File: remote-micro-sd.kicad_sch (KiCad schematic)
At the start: 0 parts

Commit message: Include adg774a component lib
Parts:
- added IC1: ADG774ABRQZ, SOP64P600X175-16N, symbol adg774a:ADG774ABRQZ
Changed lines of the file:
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@@
 	(generator_version "9.0")
 	(paper "A4")
+	(symbol
+		(lib_id "adg774a:ADG774ABRQZ")
+		(at 93.98 81.28 0)
+		(unit 1)
+		(exclude_from_sim no)
+		(in_bom yes)
+		(on_board yes)
+		(dnp no)
+		(fields_autoplaced yes)
+		(property "Reference" "IC1"
+			(at 106.68 73.66 0)
+			(effects
+				(font
+					(size 1.27 1.27)
+				)
+			)
+		)
+		(property "Value" "ADG774ABRQZ"
+			(at 106.68 76.2 0)
+			(effects
+				(font
+					(size 1.27 1.27)
+				)
+			)
+		)
+		(property "Footprint" "SOP64P600X175-16N"
+			(at 115.57 176.2 0)
+			(effects
+				(font
+					(size 1.27 1.27)
+				)
+				(justify left top)
+				(hide yes)
+			)
+		)
+		(property "Datasheet" "http://www.analog.com/media/en/technical-documentation/data-sheets/ADG774A.pdf"
+			(at 115.57 276.2 0)
+			(effects
+				(font
+					(size 1.27 1.27)
+				)
+				(justify left top)
+				(hide yes)
+			)
+		)
+		(property "Description" "ADG774ABRQZ analogue switch, QSOP16 Analog Devices ADG774ABRQZ, Analogue Switch Quad 2:1, 3.3 V, 5 V, 16-Pin QSOP"
+			(at 93.98 81.28 0)
+			(effects
+				(font
+					(size 1.27 1.27)
+				)
+				(hide yes)
+			)
+		)
+		(property "Height" "1.75"
+			(at 115.57 476.2 0)
+			(effects
+				(font
+					(size 1.27 1.27)
+				)
+				(justify left top)
+				(hide yes)
+			)
+		)
+		(property "Manufacturer_Name" "Analog Devices"
+			(at 115.57 576.2 0)
+			(effects
+				(font
+					(size 1.27 1.27)
+				)
+				(justify left top)
+				(hide yes)
+			)
+		)
+		(property "Manufacturer_Part_Number" "ADG774ABRQZ"
+			(at 115.57 676.2 0)
+			(effects
+				(font
+					(size 1.27 1.27)
+				)
+				(justify left top)
+				(hide yes)
+			)
+		)
+		(property "Mouser Part Number" "584-ADG774ABRQZ"
+			(at 115.57 776.2 0)
+			(effects
+				(font
+					(size 1.27 1.27)
+				)
+				(justify left top)
+				(hide yes)
+			)
+		)
+		(property "Mouser Price/Stock" "https://www.mouser.co.uk/ProductDetail/Analog-Devices/ADG774ABRQZ?qs=BpaRKvA4VqET7XGcXCMwIA%3D%3D"
+			(at 115.57 876.2 0)
+			(effects
+				(font
+					(size 1.27 1.27)
+				)
+				(justify left top)
+				(hide yes)
+			)
+		)
+		(property "Arrow Part Number" "ADG774ABRQZ"
+			(at 115.57 976.2 0)
+			(effects
+				(font
+					(size 1.27 1.27)
+				)
+				(justify left top)
+				(hide yes)
+			)
+		)
+		(property "Arrow Price/Stock" "https://www.arrow.com/en/products/adg774abrqz/analog-devices?region=nac"
+			(at 115.57 1076.2 0)
+			(effects
+				(font
+					(size 1.27 1.27)
+				)
+				(justify left top)
+				(hide yes)
+			)
+		)
+		(pin "16"
+		)
+		(pin "11"
+		)
+		(pin "8"
+		)
+		(pin "13"
+		)
+		(pin "10"
+		)
+		(pin "12"
+		)
+		(pin "14"
+		)
+		(pin "9"
+		)
+		(pin "15"
+		)
+		(pin "7"
+		)
+		(pin "2"
+		)
+		(pin "3"
+		)
+		(pin "4"
+		)
+		(pin "5"
+		)
+		(pin "6"
+		)
+		(pin "1"
+		)
+		(instances
+			(project ""
+				(path "/fc3ce78a-41c8-4e03-a9e4-6557f1cd3bfd"
+					(reference "IC1")
+					(unit 1)
+				)
+			)
+		)
+	)
 	(sheet_instances
 		(path "/"

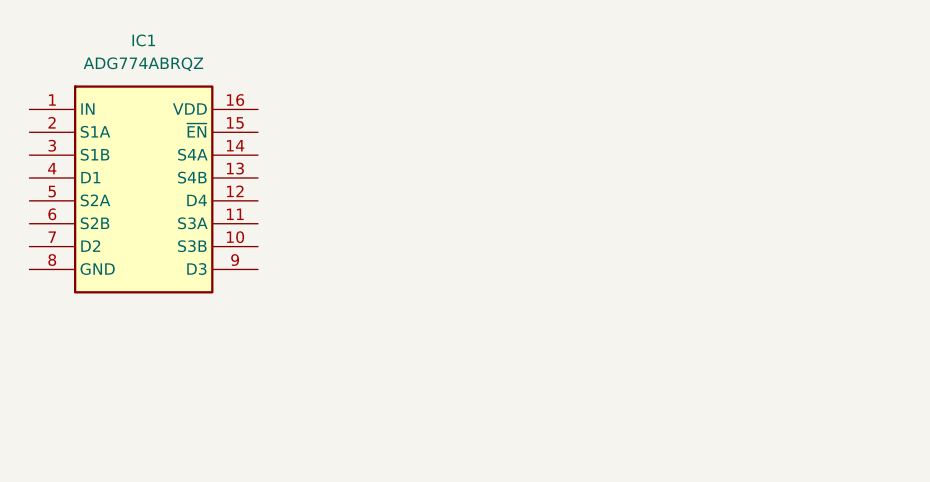
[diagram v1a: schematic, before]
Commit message: Integrate adg774a and supermini to the project
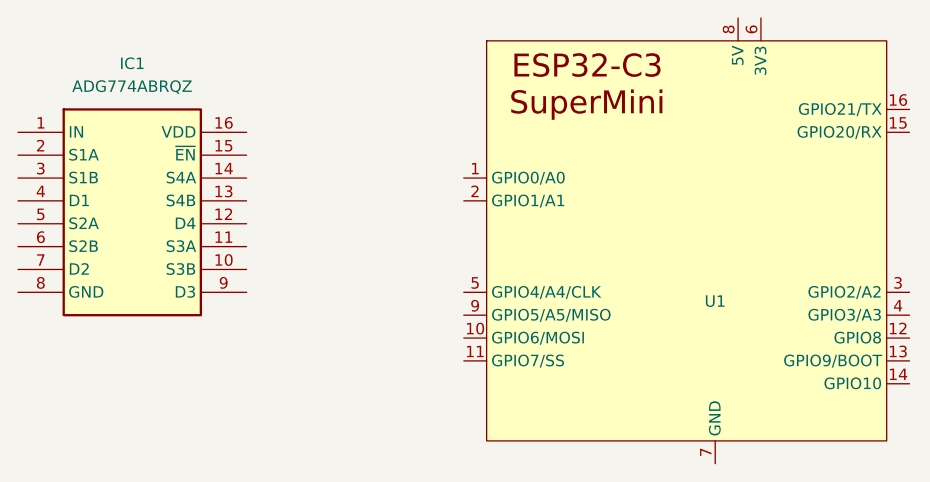
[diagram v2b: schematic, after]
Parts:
- added U1: ESP32-C3-SuperMini, esp32-c3-supermini:esp32-c3-supermini, symbol esp32-c3-supermini:esp32-c3-supermini
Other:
- moved on the sheet: IC1
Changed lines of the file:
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@@
 	(paper "A4")
 	(symbol
+		(lib_id "esp32-c3-supermini:esp32-c3-supermini")
+		(at 167.64 95.25 0)
+		(unit 1)
+		(exclude_from_sim no)
+		(in_bom yes)
+		(on_board yes)
+		(dnp no)
+		(fields_autoplaced yes)
+		(property "Reference" "U1"
+			(at 170.18 102.616 0)
+			(effects
+				(font
+					(size 1.27 1.27)
+				)
+			)
+		)
+		(property "Value" "ESP32-C3-SuperMini"
+			(at 170.18 102.87 0)
+			(effects
+				(font
+					(size 1.27 1.27)
+				)
+				(hide yes)
+			)
+		)
+		(property "Footprint" "esp32-c3-supermini:esp32-c3-supermini"
+			(at 170.18 102.87 0)
+			(effects
+				(font
+					(size 1.27 1.27)
+				)
+				(hide yes)
+			)
+		)
+		(property "Datasheet" "https://dl.artronshop.co.th/ESP32-C3%20SuperMini%20datasheet.pdf"
+			(at 170.18 102.87 0)
+			(effects
+				(font
+					(size 1.27 1.27)
+				)
+				(hide yes)
+			)
+		)
+		(property "Description" "The ESP32 C3 SuperMini is an loT mini development board based on the Espressif ESP32-C3 WiFi/ Bluetoot hdual-mode chip"
+			(at 170.18 102.87 0)
+			(effects
+				(font
+					(size 1.27 1.27)
+				)
+				(hide yes)
+			)
+		)
+		(pin "8"
+		)
+		(pin "5"
+		)
+		(pin "2"
+		)
+		(pin "1"
+		)
+		(pin "6"
+		)
+		(pin "10"
+		)
+		(pin "15"
+		)
+		(pin "4"
+		)
+		(pin "7"
+		)
+		(pin "16"
+		)
+		(pin "13"
+		)
+		(pin "11"
+		)
+		(pin "12"
+		)
+		(pin "3"
+		)
+		(pin "9"
+		)
+		(pin "14"
+		)
+		(instances
+			(project ""
+				(path "/fc3ce78a-41c8-4e03-a9e4-6557f1cd3bfd"
+					(reference "U1")
+					(unit 1)
+				)
+			)
+		)
+	)
+	(symbol
 		(lib_id "adg774a:ADG774ABRQZ")
-		(at 93.98 81.28 0)
+		(at 92.71 83.82 0)
 		(unit 1)
 		(exclude_from_sim no)
@@
 		(fields_autoplaced yes)
 		(property "Reference" "IC1"
-			(at 106.68 73.66 0)
+			(at 105.41 76.2 0)
 			(effects
 				(font
@@
 		)
 		(property "Value" "ADG774ABRQZ"
-			(at 106.68 76.2 0)
+			(at 105.41 78.74 0)
 			(effects
 				(font
@@
 		)
 		(property "Footprint" "SOP64P600X175-16N"
-			(at 115.57 176.2 0)
+			(at 114.3 178.74 0)
 			(effects
 				(font
@@
 		)
 		(property "Datasheet" "http://www.analog.com/media/en/technical-documentation/data-sheets/ADG774A.pdf"
-			(at 115.57 276.2 0)
+			(at 114.3 278.74 0)
 			(effects
 				(font
@@
 		)
 		(property "Description" "ADG774ABRQZ analogue switch, QSOP16 Analog Devices ADG774ABRQZ, Analogue Switch Quad 2:1, 3.3 V, 5 V, 16-Pin QSOP"
-			(at 93.98 81.28 0)
+			(at 92.71 83.82 0)
 			(effects
 				(font
@@
 		)
 		(property "Height" "1.75"
-			(at 115.57 476.2 0)
+			(at 114.3 478.74 0)
 			(effects
 				(font
@@
 		)
 		(property "Manufacturer_Name" "Analog Devices"
-			(at 115.57 576.2 0)
+			(at 114.3 578.74 0)
 			(effects
 				(font
@@
 		)
 		(property "Manufacturer_Part_Number" "ADG774ABRQZ"
-			(at 115.57 676.2 0)
+			(at 114.3 678.74 0)
 			(effects
 				(font
@@
 		)
 		(property "Mouser Part Number" "584-ADG774ABRQZ"
-			(at 115.57 776.2 0)
+			(at 114.3 778.74 0)
 			(effects
 				(font
@@
 		)
 		(property "Mouser Price/Stock" "https://www.mouser.co.uk/ProductDetail/Analog-Devices/ADG774ABRQZ?qs=BpaRKvA4VqET7XGcXCMwIA%3D%3D"
-			(at 115.57 876.2 0)
+			(at 114.3 878.74 0)
 			(effects
 				(font
@@
 		)
 		(property "Arrow Part Number" "ADG774ABRQZ"
-			(at 115.57 976.2 0)
+			(at 114.3 978.74 0)
 			(effects
 				(font
@@
 		)
 		(property "Arrow Price/Stock" "https://www.arrow.com/en/products/adg774abrqz/analog-devices?region=nac"
-			(at 115.57 1076.2 0)
-			(effects
-				(font
+			(at 114.3 1078.74 0)
+			(effects
+				(font
